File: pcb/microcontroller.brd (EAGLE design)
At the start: 26.2 x 26.2 mm, 8 parts

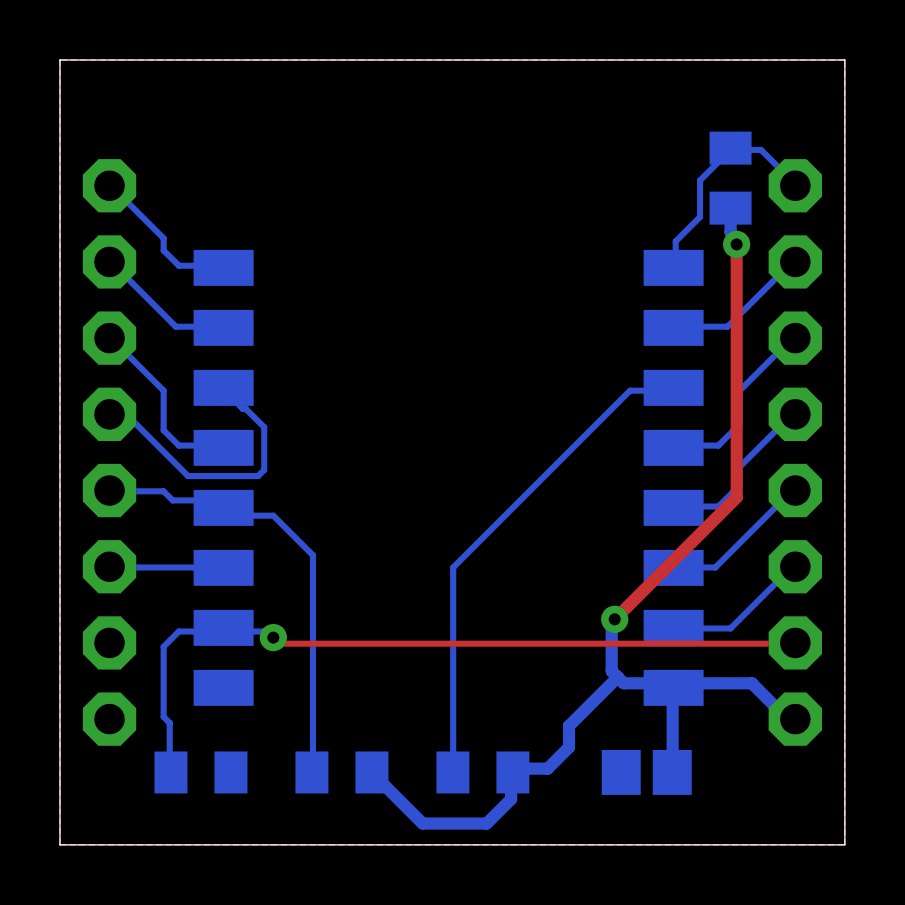
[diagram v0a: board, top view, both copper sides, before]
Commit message: Microcontroller v2 pcb ordered
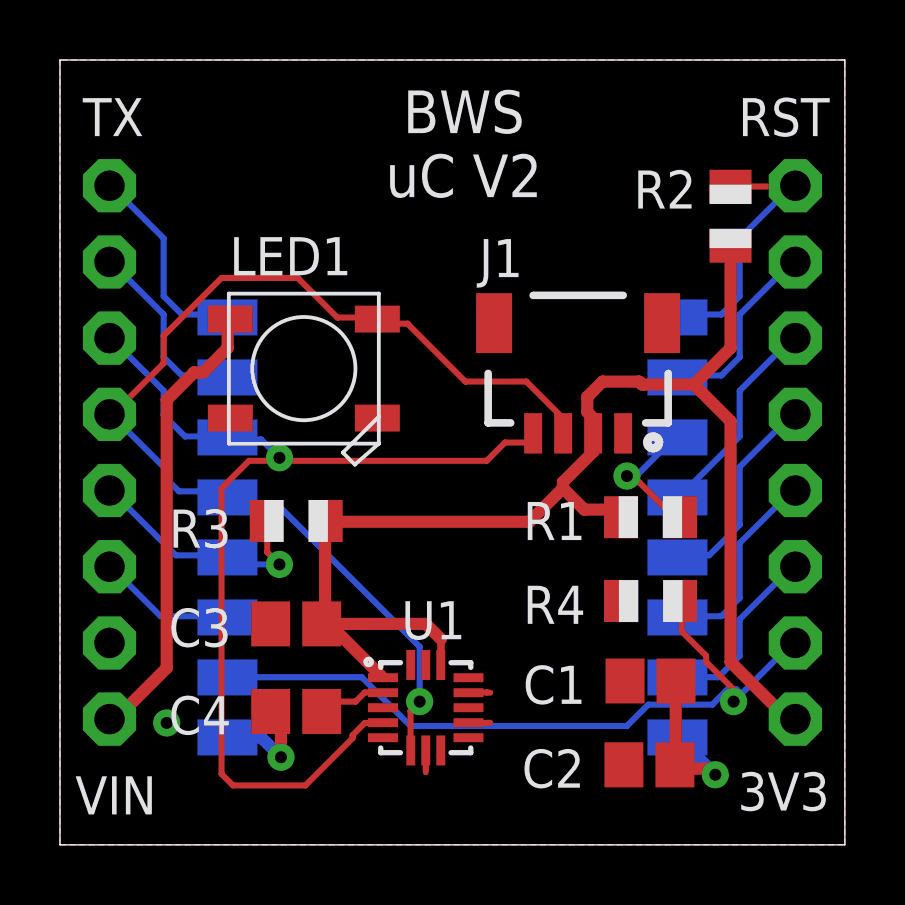
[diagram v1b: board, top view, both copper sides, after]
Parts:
- removed C10: 10uF, adafruit:C0805
- removed R10, R11, R12, R13: 10K, adafruit:R0805
- added C1, C3: 10uF, adafruit:C0805
- added C2, C4: .1uF, adafruit:C0805
- added J1: SMD, SparkX:1X04_1MM_RA
- added LED1: WS2812B5050, adafruit:WS2812B
- added R1, R2, R3, R4: 10K, adafruit:R0805
- added U$1: (no value), Twitter:TWITTER5MM
- added U1: MMA8452Q, SparkX:QFN-16_0.5MM
- moved JP1 22.9 mm to (1.65, 13.1), turned to 270 degrees
- moved JP2 22.9 mm to (24.5, 13.1), turned to 90 degrees
- moved X1 1.66 mm to (13.1, 13.1)
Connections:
- removed net +3V3: C10.1, JP1.1, R10.1, R11.1, R12.2, X1.8
- removed net 5V: JP2.8
- removed net D1/GPIO5: JP2.3, X1.13
- removed net D2/GPIO4: JP2.4, X1.14
- removed net D6/GPIO12: JP1.4, X1.6
- new net 3.3V: C3.1, J1.2, JP2.1, R1.1, R2.1, R3.2, U1.1, U1.14
- new net BYP: C4.1, U1.2
- new net D1/GPIO5/SCL: J1.4, JP1.3, U1.4, X1.14
- new net D2/GPIO4/SDA: J1.3, JP1.4, LED1.4-DIN, U1.6, X1.13
- new net D6/GPIO12/MISO: JP2.4, X1.6
- new net N$1: C1.1, C2.1, X1.8
- new net VIN: JP1.8, LED1.1-VDD
- net A0: now also JP2.7; no longer JP1.7
- net CH_PD: now also R1.2; no longer R10.2
- net D0/GPIO16: now also JP2.6; no longer JP1.6
- net D3/GPIO0: now also JP1.5, R3.1; no longer JP2.5, R12.1
- net D4/GPIO2: now also JP1.6; no longer JP2.6
- net D5/GPIO14/SCK: now also JP2.5; no longer JP1.5
- net D7/GPIO13/MOSI: now also JP2.3; no longer JP1.3
- net D8/GPIO15: now also JP2.2, R4.1; no longer JP1.2, R13.1
- net GND: now also C1.2, C2.2, C3.2, C4.2, J1.1, JP1.7, LED1.3-GND, R4.2, U1.10, U1.12, U1.5, U1.7; no longer C10.2, JP2.7, R13.2
- net RESET: now also JP2.8, R2.2; no longer JP1.8, R11.2
- net RX: now also JP1.2; no longer JP2.2
- net TX: now also JP1.1; no longer JP2.1
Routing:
- net 3.3V: track 0.00 -> 47.2 mm
- net +3V3: track 38.9 -> 0.00 mm, vias 2 -> 0
- net D2/GPIO4/SDA: track 0.00 -> 37.4 mm, vias 0 -> 1
- net D1/GPIO5/SCL: track 0.00 -> 35.2 mm, vias 0 -> 1
- net VIN: track 0.00 -> 15.3 mm
- net CH_PD: track 16.7 -> 4.59 mm, vias 0 -> 1
- net D2/GPIO4: track 9.43 -> 0.00 mm
- net D6/GPIO12/MISO: track 0.00 -> 6.84 mm
- net D3/GPIO0: track 14.9 -> 8.32 mm, vias 0 -> 1
- net D1/GPIO5: track 6.09 -> 0.00 mm
- net N$1: track 0.00 -> 6.06 mm, vias 0 -> 1
- net GND: track 0.00 -> 5.90 mm, vias 0 -> 2
- net D6/GPIO12: track 5.21 -> 0.00 mm
- net BYP: track 0.00 -> 2.31 mm
- net RESET: track 7.46 -> 9.17 mm
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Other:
- board text added: "3.3"
- board text added: "3V3"
- board text added: "A0"
- board text added: "BWS uC V2"
- board text added: "D0"
- board text added: "D1"
- board text added: "D2"
- board text added: "D3"
- board text added: "D4"
- board text added: "D5"
- board text added: "D6"
- board text added: "D7"
- board text added: "D8"
- board text added: "G"
- board text added: "RST"
- board text added: "RX"
- board text added: "TX"
- board text added: "VIN"

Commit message: Fix microcontroller board to actually connect 3.3V to the microcontroller
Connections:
- removed net N$1: C1.1, C2.1, X1.8
- net 3.3V: now also C1.1, C2.1, X1.8
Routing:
- net 3.3V: track 47.2 -> 56.7 mm, vias 0 -> 1
- net N$1: track 6.06 -> 0.00 mm, vias 1 -> 0
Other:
- board text added: "BWS uC V3"
- board text removed: "BWS uC V2"
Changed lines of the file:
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@@
 <?xml version="1.0" encoding="utf-8"?>
 <!DOCTYPE eagle SYSTEM "eagle.dtd">
-<eagle version="9.5.1">
+<eagle version="9.6.2">
 <drawing>
 <settings>
@@
 <layer number="14" name="Route14" color="1" fill="6" visible="no" active="no"/>
 <layer number="15" name="Route15" color="4" fill="6" visible="no" active="no"/>
-<layer number="16" name="Bottom" color="1" fill="1" visible="no" active="yes"/>
+<layer number="16" name="Bottom" color="1" fill="1" visible="yes" active="yes"/>
 <layer number="17" name="Pads" color="2" fill="1" visible="yes" active="yes"/>
 <layer number="18" name="Vias" color="2" fill="1" visible="yes" active="yes"/>
@@
 <layer number="20" name="Dimension" color="15" fill="1" visible="yes" active="yes"/>
 <layer number="21" name="tPlace" color="14" fill="1" visible="yes" active="yes"/>
-<layer number="22" name="bPlace" color="5" fill="1" visible="no" active="yes"/>
+<layer number="22" name="bPlace" color="5" fill="1" visible="yes" active="yes"/>
 <layer number="23" name="tOrigins" color="14" fill="1" visible="yes" active="yes"/>
-<layer number="24" name="bOrigins" color="13" fill="1" visible="no" active="yes"/>
+<layer number="24" name="bOrigins" color="13" fill="1" visible="yes" active="yes"/>
 <layer number="25" name="tNames" color="7" fill="1" visible="yes" active="yes"/>
-<layer number="26" name="bNames" color="7" fill="1" visible="no" active="yes"/>
+<layer number="26" name="bNames" color="7" fill="1" visible="yes" active="yes"/>
 <layer number="27" name="tValues" color="7" fill="1" visible="no" active="yes"/>
 <layer number="28" name="bValues" color="7" fill="1" visible="no" active="yes"/>
@@
 <layer number="38" name="bTest" color="7" fill="1" visible="no" active="yes"/>
 <layer number="39" name="tKeepout" color="4" fill="11" visible="yes" active="yes"/>
-<layer number="40" name="bKeepout" color="1" fill="11" visible="no" active="yes"/>
+<layer number="40" name="bKeepout" color="1" fill="11" visible="yes" active="yes"/>
 <layer number="41" name="tRestrict" color="4" fill="10" visible="yes" active="yes"/>
-<layer number="42" name="bRestrict" color="1" fill="10" visible="no" active="yes"/>
+<layer number="42" name="bRestrict" color="1" fill="10" visible="yes" active="yes"/>
 <layer number="43" name="vRestrict" color="2" fill="10" visible="no" active="yes"/>
 <layer number="44" name="Drills" color="7" fill="1" visible="no" active="yes"/>
@@
 <layer number="50" name="dxf" color="7" fill="1" visible="no" active="yes"/>
 <layer number="51" name="tDocu" color="7" fill="1" visible="yes" active="yes"/>
-<layer number="52" name="bDocu" color="7" fill="1" visible="no" active="yes"/>
+<layer number="52" name="bDocu" color="7" fill="1" visible="yes" active="yes"/>
 <layer number="53" name="tGND_GNDA" color="7" fill="9" visible="no" active="no"/>
 <layer number="54" name="bGND_GNDA" color="1" fill="9" visible="no" active="no"/>
@@
 </layers>
 <board>
-<fusionsync huburn="a.cGVyc29uYWw6dWUyODFhMTI5" projecturn="a.cGVyc29uYWw6dWUyODFhMTI5IzIwMTkwOTE3MjE1ODk1MzI2" f3durn="urn:adsk.wipprod:dm.lineage:P5lhZWs8S_KHtQ88bDf2NQ" pcbguid="41a5d6a7-389c-46a8-a506-c144d03ed23a" lastpulledtime="" lastsyncedchangeguid="8a204f6f-dc2d-3ee4-bfb7-58d6c85a98a5"/>
+<fusionsync huburn="a.cGVyc29uYWw6dWUyODFhMTI5" projecturn="a.cGVyc29uYWw6dWUyODFhMTI5IzIwMTkwOTE3MjE1ODk1MzI2" f3durn="urn:adsk.wipprod:dm.lineage:P5lhZWs8S_KHtQ88bDf2NQ" pcbguid="41a5d6a7-389c-46a8-a506-c144d03ed23a" lastpulledtime="" lastsyncedchangeguid="8a204f6f-dc2d-3ee4-bfb7-58d6c85a98a5" latestrevisionid="" lastsyncedrevisionid="" lastboardhashguid="" lastpushedtime="" linktopcb3d="false"/>
 <plain>
 <wire x1="0" y1="26.162" x2="0" y2="0" width="0" layer="20"/>
@@
 <text x="25.654" y="2.413" size="1.27" layer="25" font="vector" rot="R180">3V3</text>
 <text x="13.462" y="25.146" size="1.4224" layer="25" font="vector" ratio="10" align="top-center">BWS
-uC V2</text>
+uC V3</text>
 <text x="23.495" y="21.59" size="0.8128" layer="26" rot="MR0">RST</text>
 <text x="23.495" y="19.05" size="0.8128" layer="26" rot="MR0">A0</text>
@@
 <wire x1="13.716" y1="4.064" x2="13.617" y2="4.072" width="0.2032" layer="1"/>
 <wire x1="14.224" y1="4.064" x2="14.34175" y2="4.07198125" width="0.2032" layer="1"/>
-<wire x1="14.224" y1="5.08" x2="13.716" y2="5.08" width="0.2032" layer="1"/>
-<wire x1="13.716" y1="5.08" x2="13.617" y2="5.072" width="0.2032" layer="1"/>
-<wire x1="14.224" y1="5.08" x2="14.34175" y2="5.07198125" width="0.2032" layer="1"/>
+<wire x1="14.34198125" y1="5.072" x2="13.617" y2="5.072" width="0.2032" layer="1"/>
+<wire x1="14.34198125" y1="5.072" x2="14.34175" y2="5.07198125" width="0.2032" layer="1"/>
 <wire x1="7.024" y1="4.445" x2="7.366" y2="4.103" width="0.4064" layer="1"/>
 <wire x1="7.366" y1="4.103" x2="7.366" y2="2.921" width="0.4064" layer="1"/>
@@
 <wire x1="12.192" y1="7.366" x2="8.724" y2="7.366" width="0.4064" layer="1"/>
 <wire x1="10.767" y1="5.572" x2="10.7106" y2="5.6284" width="0.254" layer="1"/>
-</signal>
-<signal name="N$1" class="1">
 <contactref element="C1" pad="1"/>
 <contactref element="X1" pad="8"/>
@@
 <wire x1="20.6248" y1="2.54" x2="20.496" y2="2.667" width="0.4064" layer="1"/>
 <via x="21.844" y="2.3368" extent="1-16" drill="0.4"/>
+<wire x1="24.511" y1="4.191" x2="22.6568" y2="2.3368" width="0.4064" layer="1"/>
+<wire x1="22.6568" y1="2.3368" x2="21.844" y2="2.3368" width="0.4064" layer="1"/>
 </signal>
 <signal name="D6/GPIO12/MISO">
